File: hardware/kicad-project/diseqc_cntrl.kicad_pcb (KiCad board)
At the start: 4 copper layers, 90 x 100 mm, 127 parts, among them IC1 TPS560200DBVR, IC2 STM32F407VGT6, IC3 USBLC6-2P6, IC4 FM24CL16B-GTR, IC5 LNBH26PQR, IC6 W5500, J1 Barrel Jack, J2 Conn_01x04_Pin, J3 Conn_01x04_Pin, J4 USB4110-GF-A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

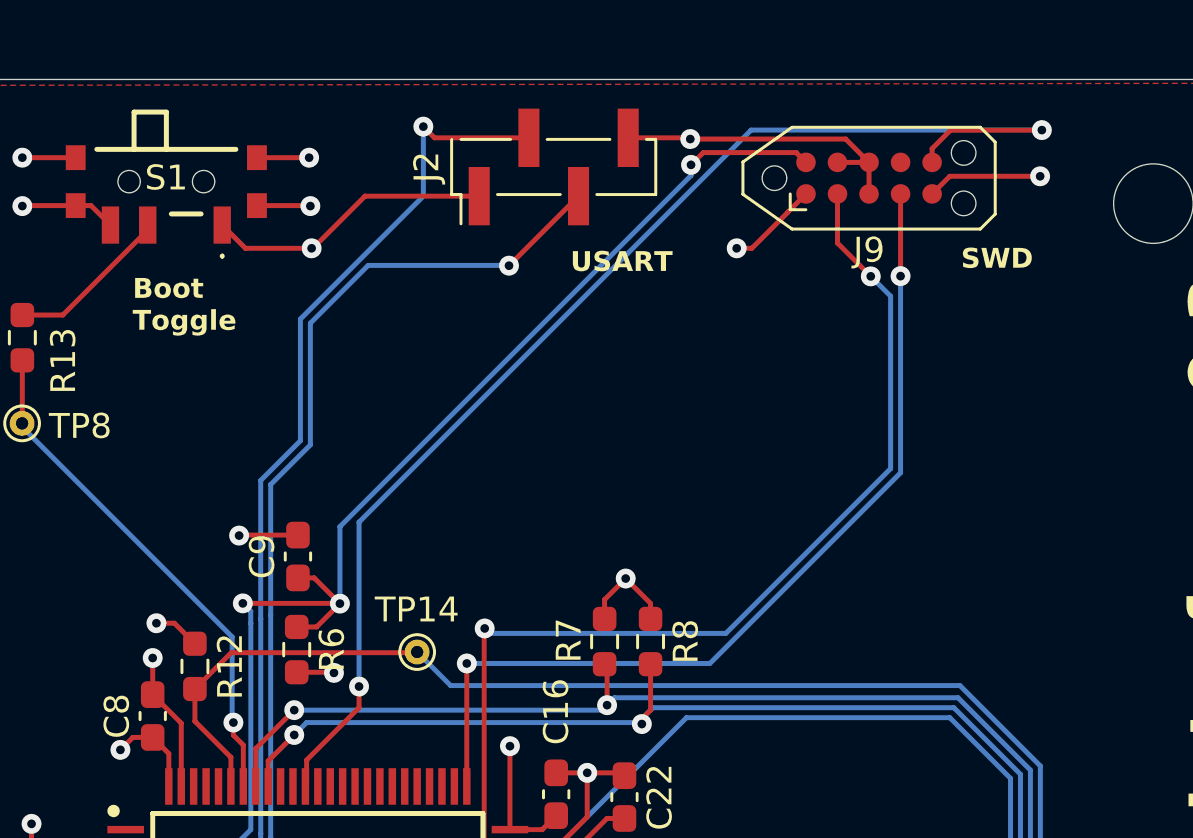
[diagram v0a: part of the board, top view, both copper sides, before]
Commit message: Added USB-UART instead of board headers
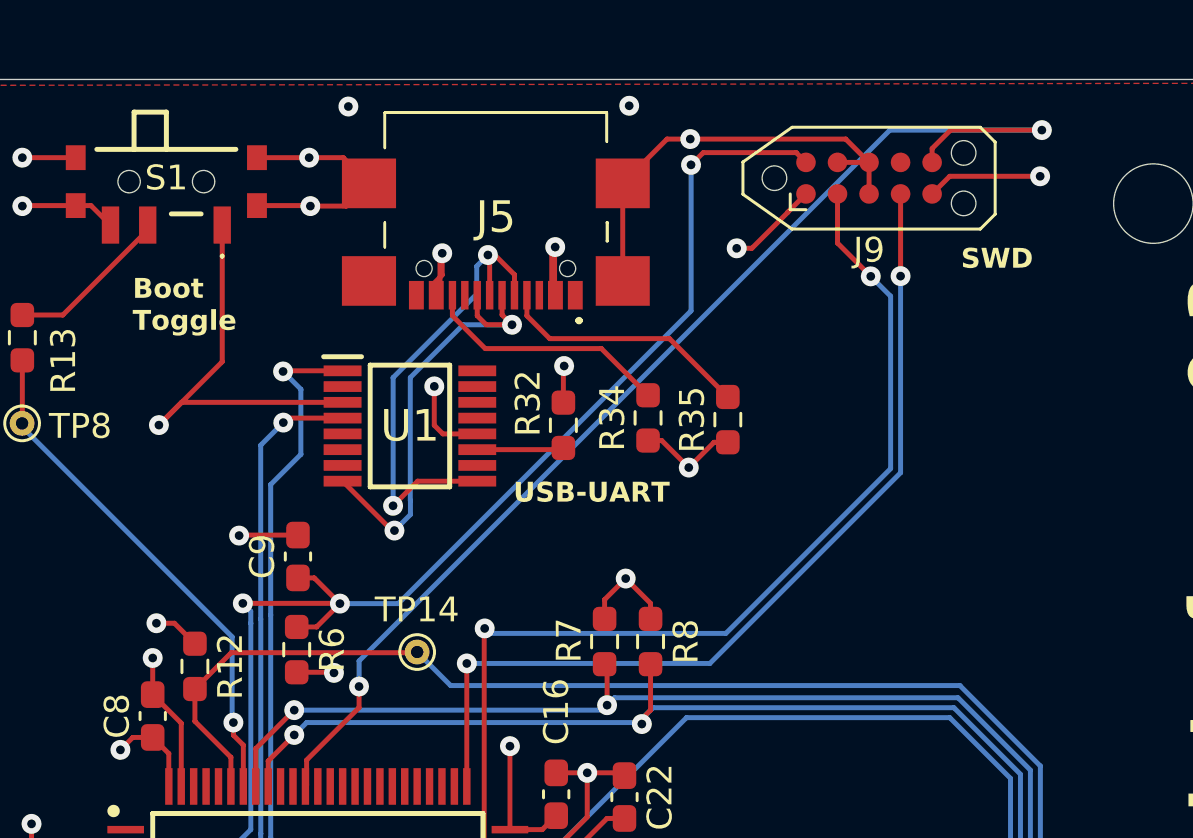
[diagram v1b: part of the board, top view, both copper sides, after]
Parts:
- removed J2: Conn_01x04_Pin, Connector_PinHeader_2.00mm:PinHeader_1x04_P2.00mm_Vertical_SMD_Pin1Left
- added J5: USB4110-GF-A, diseqc_cntrl:USB4110GFA, F.Cu at (108.5, 55.0)
- added R32: 10k, Resistor_SMD:R_0603_1608Metric_Pad0.98x0.95mm_HandSolder, F.Cu at (111.2, 63.9)
- added R34: 5k1, Resistor_SMD:R_0603_1608Metric_Pad0.98x0.95mm_HandSolder, F.Cu at (114.7, 63.6)
- added R35: 5k1, Resistor_SMD:R_0603_1608Metric_Pad0.98x0.95mm_HandSolder, F.Cu at (117.9, 63.7)
- added U1: FT230XS, diseqc_cntrl:SOP64P599X175-16N, F.Cu at (105.1, 64.0)
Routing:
- net /MCU/USB-UART/FT230_DN: track 0.00 -> 19.6 mm, vias 0 -> 2
- net /MCU/USB-UART/FT230_DP: track 0.00 -> 18.1 mm, vias 0 -> 2
- net /MCU/USART3_TX: track 58.1 -> 41.9 mm
- net GND: track 243.6 -> 258.2 mm, vias 46 -> 49
- net /MCU/USB-UART/FT230_VCC: track 0.00 -> 12.6 mm, vias 0 -> 4
- net /MCU/USART3_RX: track 56.4 -> 44.1 mm
- net +3V3: track 158.9 -> 147.0 mm
- net Net-(J5-CC1): track 0.00 -> 10.3 mm
- net Net-(J5-CC2): track 0.00 -> 10.0 mm
- net /MCU/USB-UART/FT230_RESET: track 0.00 -> 3.50 mm
- net /MCU/SWO: track 50.9 -> 47.6 mm
- net /MCU/NRST: track 57.2 -> 58.5 mm
- added copper zone on In2.Cu, net /MCU/USB-UART/FT230_VCC
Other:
- board text added: "USB-UART"
- board text removed: "USART"

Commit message: WIP: checkpoint mailbox interop investigation
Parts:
- J9: value Conn_ARM_SWD_TagConnect_TC2030 -> Conn_ARM_SWD_TagConnect_TC2050; footprint Connector:Tag-Connect_TC2050-IDC-NL_2x05_P1.27mm_Vertical -> Connector:Tag-Connect_TC2050-IDC-FP_2x05_P1.27mm_Vertical
- moved J9 0.59 mm to (123.5, 54.6)
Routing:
- net GND: track 258.2 -> 249.3 mm
- net /MCU/SWO: track 47.6 -> 44.2 mm
- net /MCU/SWCLK: track 36.8 -> 37.5 mm
- net /MCU/SWDIO: track 41.8 -> 41.2 mm
- net +3V3: track 147.0 -> 147.6 mm

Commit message: Freezing hardware v0.3
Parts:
- C9: value 100n -> 4.7n
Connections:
- J9 pad 7: unconnected-(J9-Pad7) -> GND
- J9 pad 8: GND -> unconnected-(J9-NC/TDI-Pad8)
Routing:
- net GND: track 249.3 -> 253.2 mm
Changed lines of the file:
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@@
 	(net 177 "unconnected-(IC2-PC8-Pad65)")
 	(net 178 "Net-(IC1-VSENSE)")
-	(net 179 "unconnected-(J9-Pad7)")
+	(net 179 "unconnected-(J9-NC{slash}TDI-Pad8)")
 	(net 180 "Net-(J5-CC1)")
 	(net 181 "/MCU/USB-UART/FT230_DN")
@@
 			)
 		)
-		(property "Datasheet" "https://www.tag-connect.com/wp-content/uploads/bsk-pdf-manager/TC2050-IDC-NL_Datasheet_8.pdf"
+		(property "Datasheet" "https://www.tag-connect.com/wp-content/uploads/bsk-pdf-manager/2019/12/TC2030-IDC-NL-Datasheet-Rev-B.pdf"
 			(at 0 0 0)
 			(unlocked yes)
@@
 			)
 		)
-		(property "Description" "Tag-Connect’s 10-pins connector"
+		(property "Description" "Header, Tagconnect, 2x5, Cortex-M"
 			(at 0 0 0)
 			(unlocked yes)
@@
 			)
 		)
-		(property ki_fp_filters "*TC2050*")
+		(property ki_fp_filters "TC2050*")
 		(sheetname "/MCU/")
 		(sheetfile "diseqc_cntrl_mcu.kicad_sch")
-		(attr exclude_from_pos_files exclude_from_bom)
+		(attr exclude_from_pos_files)
 		(fp_line
 			(start -3.175 1.27)
@@
 			(layers "F.Cu" "F.Mask")
 			(net 2 "+3V3")
+			(pinfunction "VCC")
 			(pintype "passive")
 		)
@@
 			(layers "F.Cu" "F.Mask")
 			(net 21 "/MCU/SWDIO")
+			(pinfunction "SWDIO/TMS")
 			(pintype "passive")
 		)
@@
 			(layers "F.Cu" "F.Mask")
 			(net 1 "GND")
+			(pinfunction "GND")
 			(pintype "passive")
 		)
@@
 			(layers "F.Cu" "F.Mask")
 			(net 17 "/MCU/SWCLK")
+			(pinfunction "SWDCLK/TCK")
 			(pintype "passive")
 		)
@@
 			(layers "F.Cu" "F.Mask")
 			(net 1 "GND")
+			(pinfunction "(GND)/(Vcc5V)")
 			(pintype "passive")
 		)
@@
 			(layers "F.Cu" "F.Mask")
 			(net 23 "/MCU/SWO")
+			(pinfunction "SWO/TDO")
 			(pintype "passive")
 		)
@@
 			(size 0.7874 0.7874)
 			(layers "F.Cu" "F.Mask")
-			(net 179 "unconnected-(J9-Pad7)")
-			(pintype "passive+no_connect")
+			(net 1 "GND")
+			(pinfunction "(key)")
+			(pintype "passive")
 		)
 		(pad "8" connect circle
@@
 			(size 0.7874 0.7874)
 			(layers "F.Cu" "F.Mask")
-			(net 1 "GND")
-			(pintype "passive")
+			(net 179 "unconnected-(J9-NC{slash}TDI-Pad8)")
+			(pinfunction "NC/TDI")
+			(pintype "passive+no_connect")
 		)
 		(pad "9" connect circle
@@
 			(layers "F.Cu" "F.Mask")
 			(net 1 "GND")
+			(pinfunction "GND/nTRST")
 			(pintype "passive")
 		)
@@
 			(layers "F.Cu" "F.Mask")
 			(net 3 "/MCU/NRST")
+			(pinfunction "nRESET")
 			(pintype "passive")
 		)
@@
 			)
 		)
-		(property "Value" "100n"
+		(property "Value" "4.7n"
 			(at 0 1.43 90)
 			(layer "F.Fab")
@@
 		(sheetname "/MCU/")
 		(sheetfile "diseqc_cntrl_mcu.kicad_sch")
-		(attr smd)
+		(attr smd dnp)
 		(fp_line
 			(start -0.146267 -0.51)
@@
 	)
 	(segment
-		(start 123.54 55.195)
-		(end 123.54 53.925)
-		(width 0.2)
-		(layer "F.Cu")
-		(net 1)
-	)
-	(segment
 		(start 95.85 78.474)
 		(end 95.85 75.925)
@@
 	)
 	(segment
+		(start 123.54 55.195)
+		(end 124.81 53.925)
+		(width 0.2)
+		(layer "F.Cu")
+		(net 1)
+	)
+	(segment
 		(start 52.54 86.38)
 		(end 52.54 82.985)
@@
 	)
 	(segment
+		(start 122.96 52.075)
+		(end 122.96 51.88)
+		(width 0.2)
+		(layer "F.Cu")
+		(net 1)
+	)
+	(segment
 		(start 94.801 116.299)
 		(end 94.7 116.4)
@@
 	)
 	(segment
+		(start 122.27 53.925)
+		(end 123.54 55.195)
+		(width 0.2)
+		(layer "F.Cu")
+		(net 1)
+	)
+	(segment
 		(start 125 84.5)
 		(end 127.05 84.5)
@@
 	)
 	(segment
-		(start 122.27 53.925)
-		(end 123.54 53.925)
-		(width 0.2)
-		(layer "F.Cu")
-		(net 1)
-	)
-	(segment
 		(start 101 53.15)
 		(end 102.375 53.15)
@@
 	)
 	(segment
+		(start 124.81 53.925)
+		(end 122.96 52.075)
+		(width 0.2)
+		(layer "F.Cu")
+		(net 1)
+	)
+	(segment
 		(start 62.4 60.05)
 		(end 63.85 58.6)
@@
 	)
 	(segment
-		(start 123.313321 59.759402)
-		(end 123.313321 56.691679)
+		(start 123.9 56.105)
+		(end 124.81 55.195)
 		(width 0.2)
 		(layer "F.Cu")
@@
 	)
 	(segment
-		(start 123.313321 56.691679)
-		(end 124.81 55.195)
+		(start 123.9 59.172723)
+		(end 123.9 56.105)
+		(width 0.2)
+		(layer "F.Cu")
+		(net 17)
+	)
+	(segment
+		(start 123.313321 59.759402)
+		(end 123.9 59.172723)
 		(width 0.2)
 		(layer "F.Cu")
@@
 		(width 0.2)
 		(layer "F.Cu")
-		(net 182)
-	)
-	(segment
-		(start 111.26 62.995)
-		(end 111.24 63.015)
-		(width 0.2)
-		(layer "F.Cu")

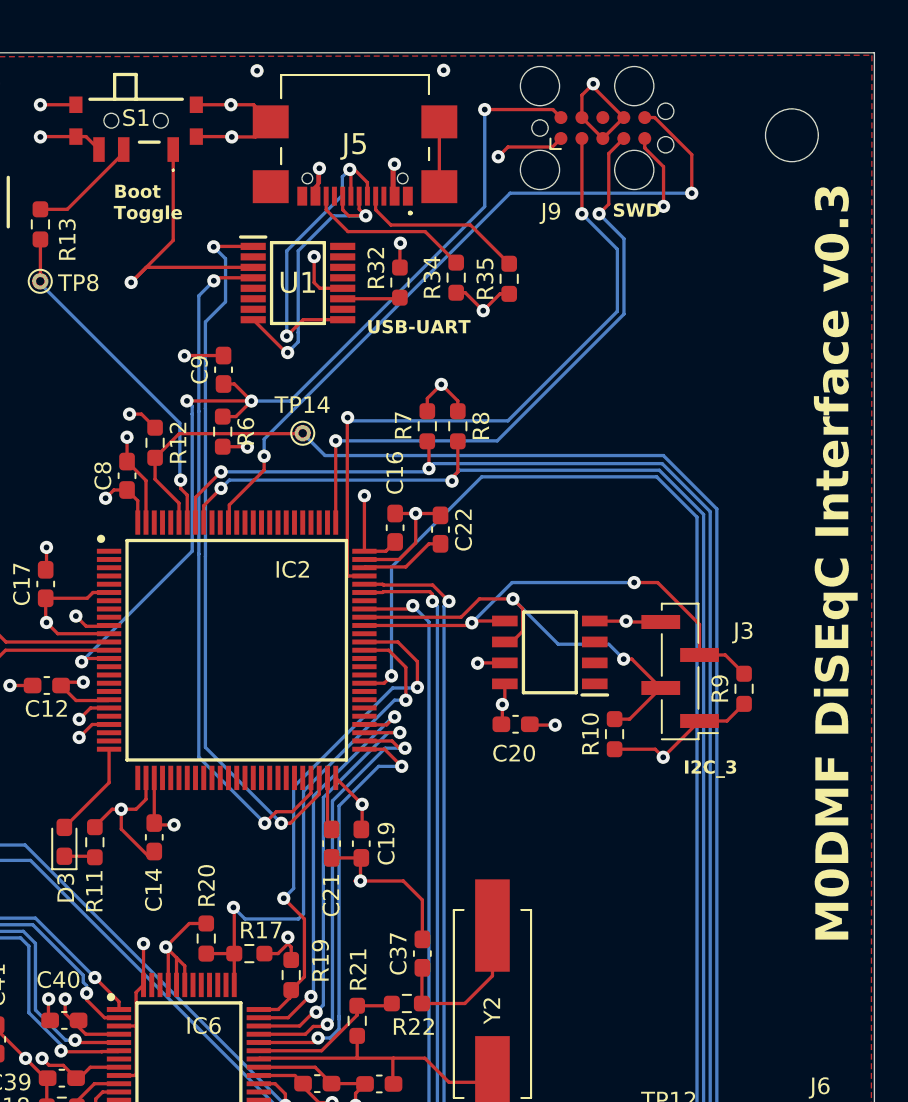
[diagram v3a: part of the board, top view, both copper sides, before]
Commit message: Starting v0.4 with FT230 fixes; extra TPs
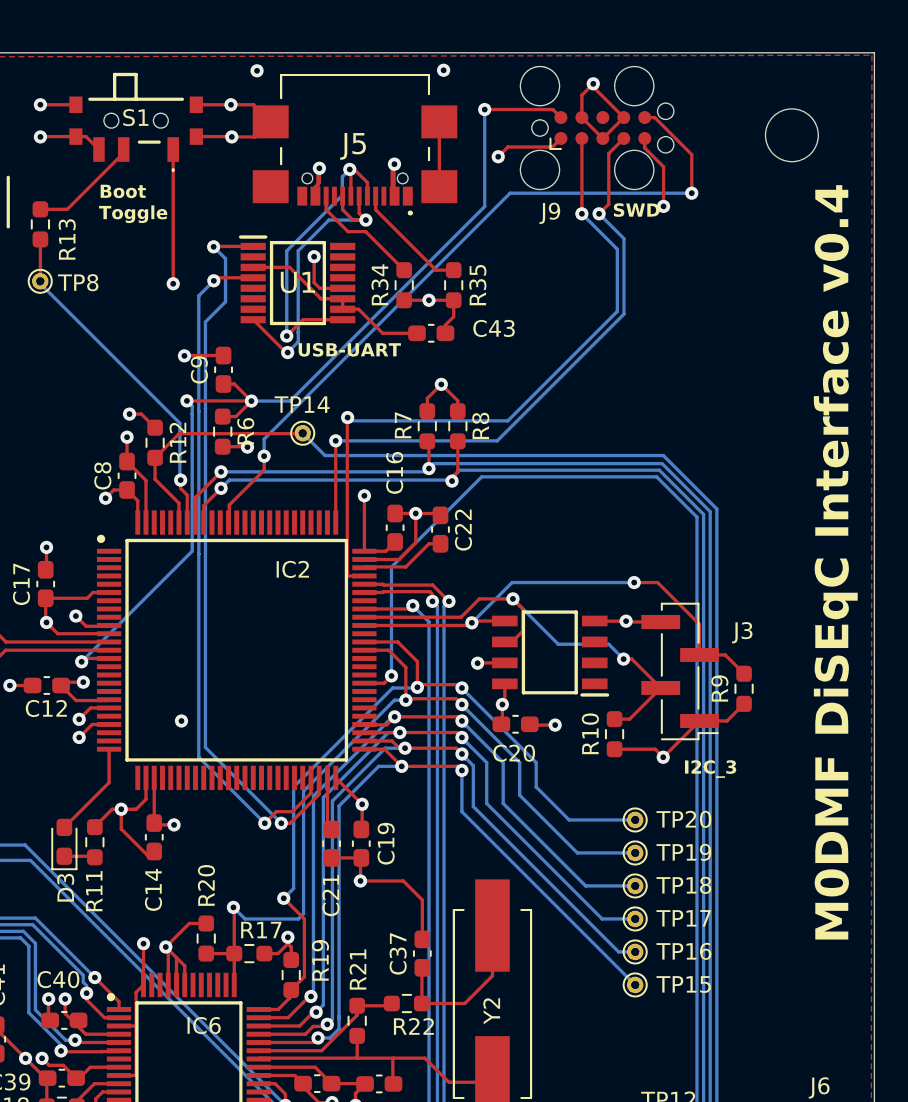
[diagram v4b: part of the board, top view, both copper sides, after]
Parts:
- removed R32: 10k, Resistor_SMD:R_0603_1608Metric_Pad0.98x0.95mm_HandSolder
- added C43: 100n, Capacitor_SMD:C_0603_1608Metric_Pad1.08x0.95mm_HandSolder, F.Cu at (113.1, 67.0)
- added TP15: TP_SCSN, TestPoint:TestPoint_THTPad_D1.0mm_Drill0.5mm, F.Cu at (125.5, 106.5)
- added TP16: TP_SCLK, TestPoint:TestPoint_THTPad_D1.0mm_Drill0.5mm, F.Cu at (125.5, 104.5)
- added TP17: TP_MISO, TestPoint:TestPoint_THTPad_D1.0mm_Drill0.5mm, F.Cu at (125.5, 102.5)
- added TP18: TP_MOSI, TestPoint:TestPoint_THTPad_D1.0mm_Drill0.5mm, F.Cu at (125.5, 100.5)
- added TP19: TP_W5500_RST, TestPoint:TestPoint_THTPad_D1.0mm_Drill0.5mm, F.Cu at (125.5, 98.5)
- added TP20: TP_W5500_RST, TestPoint:TestPoint_THTPad_D1.0mm_Drill0.5mm, F.Cu at (125.5, 96.5)
- C28, C30: value 220n -> 200n
- moved R35 3.38 mm to (114.5, 64.1)
- moved R34 3.18 mm to (111.5, 64.1)
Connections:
- net /MCU/W5500 Ethernet/MISO renamed /MCU/MISO
- net /MCU/W5500 Ethernet/MOSI renamed /MCU/MOSI
- net /MCU/W5500 Ethernet/SCLK renamed /MCU/SCLK
- net /MCU/W5500 Ethernet/SCSN renamed /MCU/SCSN
- net /MCU/W5500 Ethernet/W5500_INT renamed /MCU/W5500_INT
- net /MCU/W5500 Ethernet/W5500_RST renamed /MCU/W5500_RST
- U1 pad 10: unconnected-(U1-3V3OUT-Pad10) -> Net-(U1-3V3OUT)
- U1 pad 11: /MCU/USB-UART/FT230_RESET -> Net-(U1-3V3OUT)
- U1 pad 3: +3V3 -> Net-(U1-3V3OUT)
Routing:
- net /MCU/SCSN: track 26.2 -> 47.3 mm, vias 2 -> 3
- net /MCU/SCLK: track 26.5 -> 47.2 mm, vias 2 -> 3
- net /MCU/MISO: track 25.4 -> 46.0 mm, vias 2 -> 3
- net /MCU/MOSI: track 24.9 -> 45.3 mm, vias 2 -> 3
- net /MCU/W5500_RST: track 31.9 -> 51.1 mm, vias 2 -> 3
- net /MCU/W5500_INT: track 31.5 -> 49.0 mm, vias 2 -> 3
- net Net-(U1-3V3OUT): track 0.00 -> 12.0 mm
- net +3V3: track 147.6 -> 138.8 mm
- net /MCU/USB-UART/FT230_RESET: track 3.50 -> 0.00 mm
- net Net-(J5-CC1): track 10.3 -> 7.07 mm
- net Net-(J5-CC2): track 10.0 -> 7.07 mm
- net /MCU/USB-UART/FT230_VCC: track 12.5 -> 11.0 mm, vias 4 -> 3
- net GND: track 253.2 -> 254.3 mm, vias 49 -> 50
- net /MCU/USB-UART/FT230_DP: track 18.1 -> 18.7 mm
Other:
- board text added: "M0DMF DiSEqC Interface v0.4"
- board text removed: "M0DMF DiSEqC Interface v0.3"

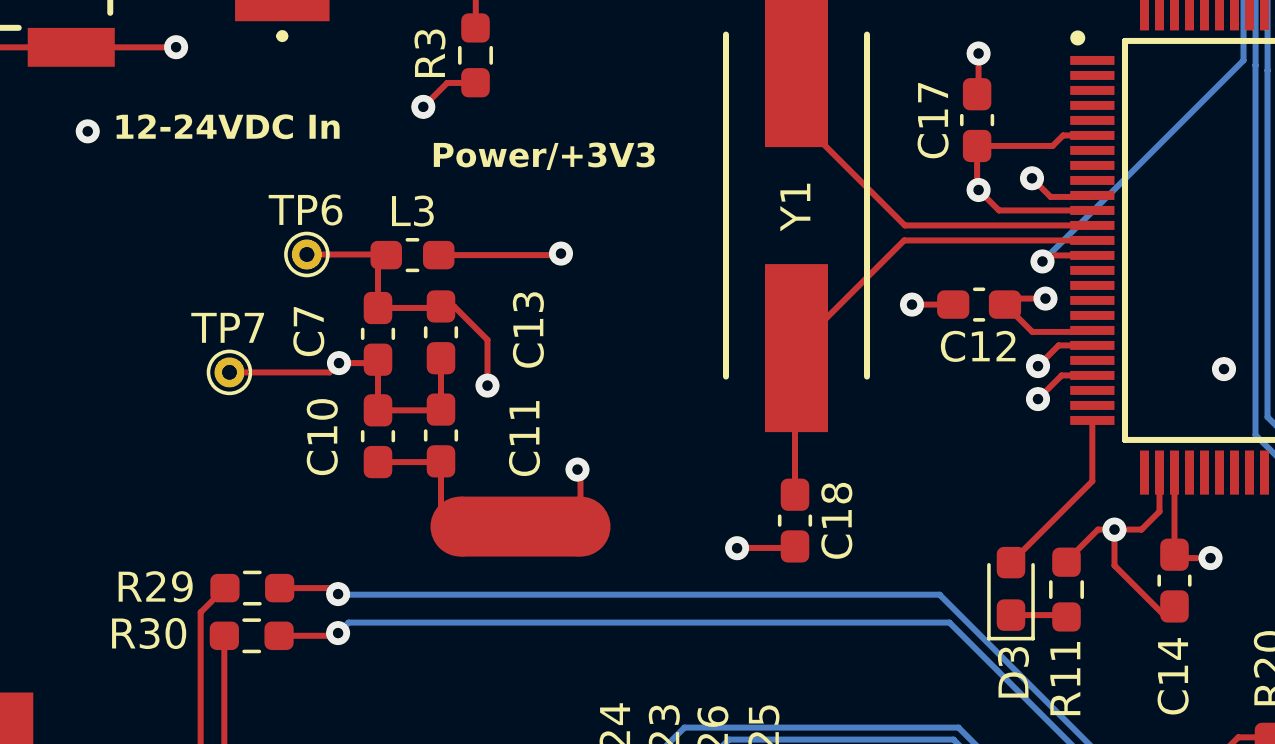
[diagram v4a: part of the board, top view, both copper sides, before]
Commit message: Removed separate VDDA/VSSA planes
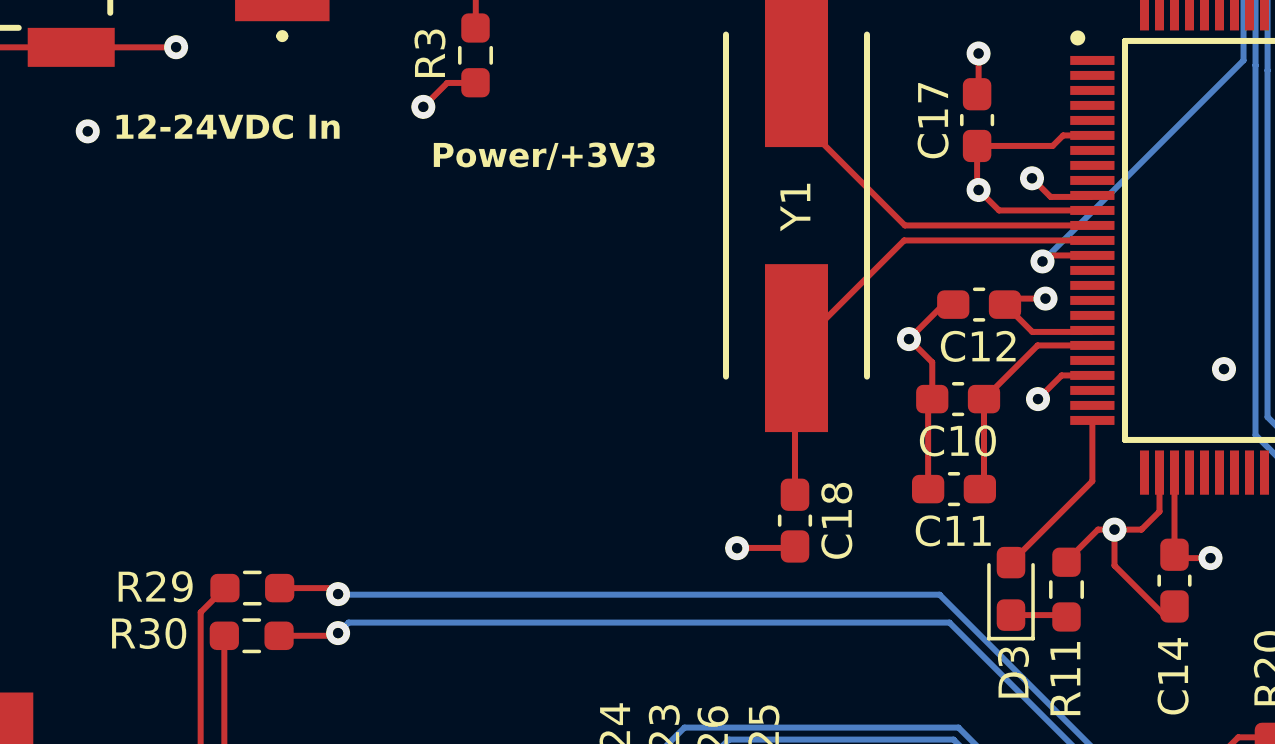
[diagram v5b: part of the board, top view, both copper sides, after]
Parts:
- removed C13: 10n, Capacitor_SMD:C_0603_1608Metric_Pad1.08x0.95mm_HandSolder
- removed C7: 1u, Capacitor_SMD:C_0603_1608Metric_Pad1.08x0.95mm_HandSolder
- removed L3: 39n, Inductor_SMD:L_0603_1608Metric_Pad1.05x0.95mm_HandSolder
- removed NT1: NetTie_2, NetTie:NetTie-2_SMD_Pad2.0mm
- removed TP6: TP_3V3_ANA, TestPoint:TestPoint_THTPad_D1.0mm_Drill0.5mm
- removed TP7: TP_VSSA, TestPoint:TestPoint_THTPad_D1.0mm_Drill0.5mm
- moved C10 19.4 mm to (89.1, 91.5), turned to 180 degrees
- moved C11 17.2 mm to (89.0, 94.5), turned to 180 degrees
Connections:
- net VSSA renamed /MCU/VSSA
- C10 pad 2: Net-(C10-Pad2) -> GND
- C11 pad 2: Net-(C10-Pad2) -> GND
- IC2 pad 22: +3V3_ANA -> +3V3
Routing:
- net +3V3_ANA: track 30.3 -> 0.00 mm, vias 2 -> 0
- net /MCU/VSSA: track 36.1 -> 7.41 mm, vias 2 -> 0
- net Net-(C10-Pad2): track 4.55 -> 0.00 mm
- net GND: track 254.3 -> 258.3 mm, vias 50 -> 49
- net +3V3: track 138.8 -> 136.9 mm
- removed copper zone on In2.Cu, net +3V3_ANA
- removed copper zone on In1.Cu, net /MCU/VSSA
